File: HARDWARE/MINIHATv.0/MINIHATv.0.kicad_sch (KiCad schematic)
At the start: 0 parts

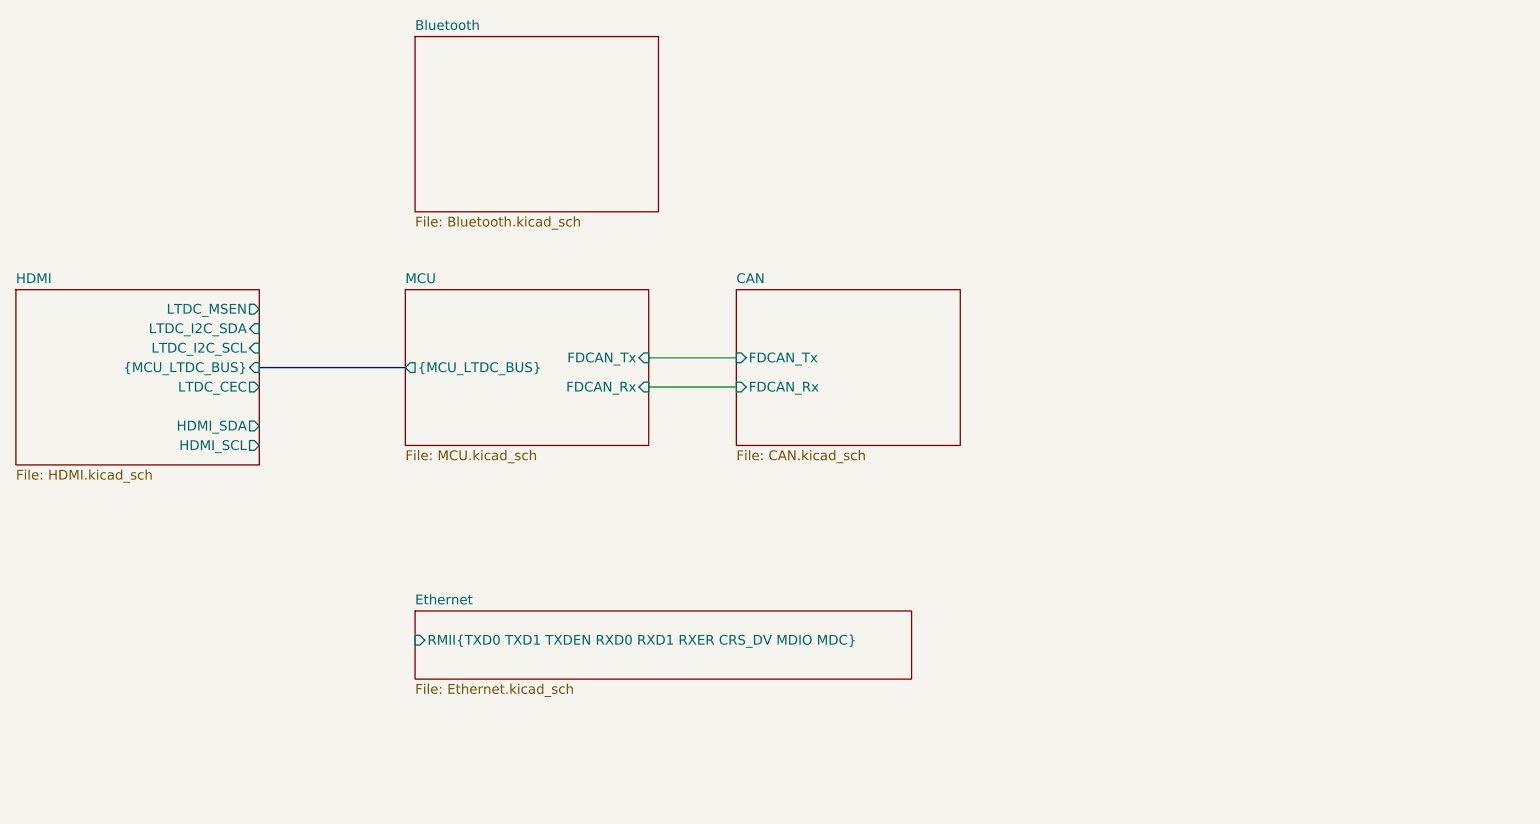
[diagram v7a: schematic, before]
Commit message: boot sw, top page bt added
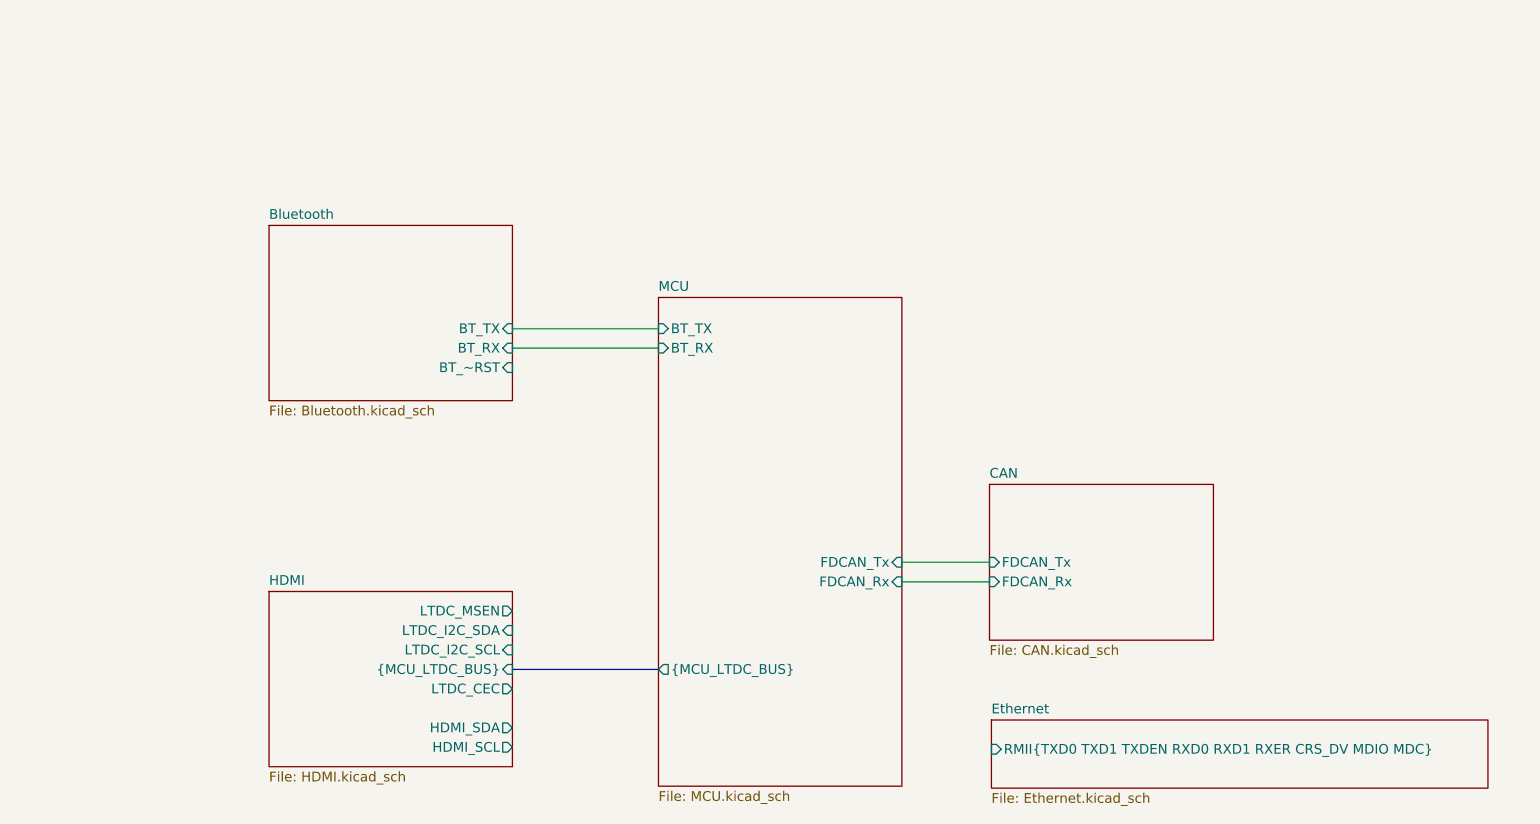
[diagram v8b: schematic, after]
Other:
- sheet Bluetooth ports: added BT_RX, BT_TX, BT_~RST; removed none
- sheet MCU ports: added BT_RX, BT_TX; removed none
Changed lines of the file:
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@@
 	(wire
 		(pts
-			(xy 127 59.69) (xy 138.43 59.69)
+			(xy 109.22 58.42) (xy 128.27 58.42)
 		)
 		(stroke
@@
 	(wire
 		(pts
-			(xy 127 63.5) (xy 138.43 63.5)
+			(xy 160.02 86.36) (xy 171.45 86.36)
 		)
 		(stroke
@@
 		)
 	)
+	(wire
+		(pts
+			(xy 109.22 55.88) (xy 128.27 55.88)
+		)
+		(stroke
+			(width 0)
+			(type default)
+		)
+	)
+	(wire
+		(pts
+			(xy 160.02 88.9) (xy 171.45 88.9)
+		)
+		(stroke
+			(width 0)
+			(type default)
+		)
+	)
 	(bus
 		(pts
-			(xy 76.2 60.96) (xy 95.25 60.96)
+			(xy 109.22 100.33) (xy 128.27 100.33)
 		)
 		(stroke
@@
 	)
 	(sheet
-		(at 96.52 17.78)
+		(at 77.47 42.418)
 		(size 31.75 22.86)
 		(exclude_from_sim no)
@@
 		)
 		(property "Sheetname" "Bluetooth"
-			(at 96.52 17.0684 0)
+			(at 77.47 41.7064 0)
 			(show_name no)
 			(do_not_autoplace no)
@@
 		)
 		(property "Sheetfile" "Bluetooth.kicad_sch"
-			(at 96.52 41.2246 0)
+			(at 77.47 65.8626 0)
 			(show_name no)
 			(do_not_autoplace no)
@@
 				)
 				(justify left top)
+			)
+		)
+		(pin "BT_RX" input
+			(at 109.22 58.42 0)
+			(effects
+				(font
+					(size 1.27 1.27)
+				)
+				(justify right)
+			)
+		)
+		(pin "BT_TX" input
+			(at 109.22 55.88 0)
+			(effects
+				(font
+					(size 1.27 1.27)
+				)
+				(justify right)
+			)
+		)
+		(pin "BT_~RST" input
+			(at 109.22 60.96 0)
+			(effects
+				(font
+					(size 1.27 1.27)
+				)
+				(justify right)
 			)
 		)
@@
 	)
 	(sheet
-		(at 138.43 50.8)
+		(at 171.45 76.2)
 		(size 29.21 20.32)
 		(exclude_from_sim no)
@@
 		)
 		(property "Sheetname" "CAN"
-			(at 138.43 50.0884 0)
+			(at 171.45 75.4884 0)
 			(show_name no)
 			(do_not_autoplace no)
@@
 		)
 		(property "Sheetfile" "CAN.kicad_sch"
-			(at 138.43 71.7046 0)
+			(at 171.45 97.1046 0)
 			(show_name no)
 			(do_not_autoplace no)
@@
 		)
 		(pin "FDCAN_Rx" input
-			(at 138.43 63.5 180)
+			(at 171.45 88.9 180)
 			(effects
 				(font
@@
 		)
 		(pin "FDCAN_Tx" input
-			(at 138.43 59.69 180)
+			(at 171.45 86.36 180)
 			(effects
 				(font
@@
 	)
 	(sheet
-		(at 44.45 50.8)
+		(at 77.47 90.17)
 		(size 31.75 22.86)
 		(exclude_from_sim no)
@@
 		)
 		(property "Sheetname" "HDMI"
-			(at 44.45 50.0884 0)
+			(at 77.47 89.4584 0)
 			(show_name no)
 			(do_not_autoplace no)
@@
 		)
 		(property "Sheetfile" "HDMI.kicad_sch"
-			(at 44.45 74.2446 0)
+			(at 77.47 113.6146 0)
 			(show_name no)
 			(do_not_autoplace no)
@@
 		)
 		(pin "{MCU_LTDC_BUS}" input
-			(at 76.2 60.96 0)
+			(at 109.22 100.33 0)
 			(effects
 				(font
@@
 		)
 		(pin "HDMI_SCL" output
-			(at 76.2 71.12 0)
+			(at 109.22 110.49 0)
 			(effects
 				(font
@@
 		)
 		(pin "HDMI_SDA" output
-			(at 76.2 68.58 0)
+			(at 109.22 107.95 0)
 			(effects
 				(font
@@
 		)
 		(pin "LTDC_CEC" output
-			(at 76.2 63.5 0)
+			(at 109.22 102.87 0)
 			(effects
 				(font
@@
 		)
 		(pin "LTDC_I2C_SCL" input
-			(at 76.2 58.42 0)
+			(at 109.22 97.79 0)
 			(effects
 				(font
@@
 		)
 		(pin "LTDC_I2C_SDA" input
-			(at 76.2 55.88 0)
+			(at 109.22 95.25 0)
 			(effects
 				(font
@@
 		)
 		(pin "LTDC_MSEN" output
-			(at 76.2 53.34 0)
+			(at 109.22 92.71 0)
 			(effects
 				(font
@@
 	)
 	(sheet
-		(at 96.52 92.71)
+		(at 171.704 106.934)
 		(size 64.77 8.89)
 		(exclude_from_sim no)
@@
 		)
 		(property "Sheetname" "Ethernet"
-			(at 96.52 91.9984 0)
+			(at 171.704 106.2224 0)
 			(show_name no)
 			(do_not_autoplace no)
@@
 		)
 		(property "Sheetfile" "Ethernet.kicad_sch"
-			(at 96.52 102.1846 0)
+			(at 171.704 116.4086 0)
 			(show_name no)
 			(do_not_autoplace no)
@@
 		)
 		(pin "RMII{TXD0 TXD1 TXDEN RXD0 RXD1 RXER CRS_DV MDIO MDC}" input
-			(at 96.52 96.52 180)
+			(at 171.704 110.744 180)
 			(effects
 				(font
@@
 	)
 	(sheet
-		(at 95.25 50.8)
-		(size 31.75 20.32)
+		(at 128.27 51.816)
+		(size 31.75 63.754)
 		(exclude_from_sim no)
 		(in_bom yes)
@@
 		)
 		(property "Sheetname" "MCU"
-			(at 95.25 50.0884 0)
+			(at 128.27 51.1044 0)
 			(show_name no)
 			(do_not_autoplace no)
@@
 		)
 		(property "Sheetfile" "MCU.kicad_sch"
-			(at 95.25 71.7046 0)
+			(at 128.27 116.1546 0)
 			(show_name no)
 			(do_not_autoplace no)
@@
 		)
 		(pin "FDCAN_Rx" input
-			(at 127 63.5 0)
+			(at 160.02 88.9 0)
 			(effects
 				(font
@@
 		)
 		(pin "FDCAN_Tx" input
-			(at 127 59.69 0)
+			(at 160.02 86.36 0)
 			(effects
 				(font
@@
 		)
 		(pin "{MCU_LTDC_BUS}" output
-			(at 95.25 60.96 180)
-			(effects
-				(font
+			(at 128.27 100.33 180)
+			(effects
+				(font
+					(size 1.27 1.27)
+				)
+				(justify left)
+			)
+		)
+		(pin "BT_RX" input
+			(at 128.27 58.42 180)
+			(effects
+				(font
+					(size 1.27 1.27)
+				)
+				(justify left)
+			)
+		)
+		(pin "BT_TX" input
+			(at 128.27 55.88 180)
+			(effects
+				(font
